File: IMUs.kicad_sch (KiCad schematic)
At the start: 15 parts, among them U501 LSM6DSL, U502 BMP390

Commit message: feat: add layout notes and net labels
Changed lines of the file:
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@@
+		)
+	)
+	(text_box "Place away from connectors, mounting holes & switching circuits."
+		(exclude_from_sim no)
+		(at 115.57 124.1808 0)
+		(size 70.485 8.773)
+		(margins 0.9525 0.9525 0.9525 0.9525)
+		(stroke
+			(width 0)
+			(type solid)
+		)
+		(fill
+			(type none)
+		)
+		(effects
+			(font
+				(face "Adwaita Sans")
+				(size 2.032 2.032)
+				(bold yes)
+			)
+			(justify left top)
 		)
 	)

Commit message: refactor: change name from FeroFly405 to FeroFlyF405
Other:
- title: FeroFly405 -> FeroFlyF405
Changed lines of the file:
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@@
 	(paper "A4")
 	(title_block
-		(title "FeroFly405")
+		(title "FeroFlyF405")
 		(date "2026-07-22")
 		(rev "1")
-		(comment 3 "GitHub: https://github.com/Ozonised/FeroFly405")
+		(comment 3 "GitHub: https://github.com/Ozonised/FeroFlyF405")
 		(comment 4 "Designed by: Farhan Khan")
 	)
@@
 		)
 		(instances
-			(project "FeroFly"
+			(project "FeroFlyF405"
 				(path "/8fea5468-8d8d-4bdb-afc0-e65b62c92669/2db1372a-2ed6-420c-af8b-d4f9c1346569/bd7b114a-6246-4c5b-8567-24e6abe0f316"
 					(reference "U501")
@@
 		)
 		(instances
-			(project "FeroFly"
+			(project "FeroFlyF405"
 				(path "/8fea5468-8d8d-4bdb-afc0-e65b62c92669/2db1372a-2ed6-420c-af8b-d4f9c1346569/bd7b114a-6246-4c5b-8567-24e6abe0f316"
 					(reference "#PWR0404")
@@
 		)
 		(instances
-			(project "FeroFly"
+			(project "FeroFlyF405"
 				(path "/8fea5468-8d8d-4bdb-afc0-e65b62c92669/2db1372a-2ed6-420c-af8b-d4f9c1346569/bd7b114a-6246-4c5b-8567-24e6abe0f316"
 					(reference "TP505")
@@
 		)
 		(instances
-			(project "FeroFly"
+			(project "FeroFlyF405"
 				(path "/8fea5468-8d8d-4bdb-afc0-e65b62c92669/2db1372a-2ed6-420c-af8b-d4f9c1346569/bd7b114a-6246-4c5b-8567-24e6abe0f316"
 					(reference "#PWR0407")
@@
 		)
 		(instances
-			(project "FeroFly"
+			(project "FeroFlyF405"
 				(path "/8fea5468-8d8d-4bdb-afc0-e65b62c92669/2db1372a-2ed6-420c-af8b-d4f9c1346569/bd7b114a-6246-4c5b-8567-24e6abe0f316"
 					(reference "C502")
@@
 		)
 		(instances
-			(project "FeroFly"
+			(project "FeroFlyF405"
 				(path "/8fea5468-8d8d-4bdb-afc0-e65b62c92669/2db1372a-2ed6-420c-af8b-d4f9c1346569/bd7b114a-6246-4c5b-8567-24e6abe0f316"
 					(reference "#PWR0409")
@@
 		)
 		(instances
-			(project "FeroFly"
+			(project "FeroFlyF405"
 				(path "/8fea5468-8d8d-4bdb-afc0-e65b62c92669/2db1372a-2ed6-420c-af8b-d4f9c1346569/bd7b114a-6246-4c5b-8567-24e6abe0f316"
 					(reference "#PWR0411")
@@
 		)
 		(instances
-			(project "FeroFly"
+			(project "FeroFlyF405"
 				(path "/8fea5468-8d8d-4bdb-afc0-e65b62c92669/2db1372a-2ed6-420c-af8b-d4f9c1346569/bd7b114a-6246-4c5b-8567-24e6abe0f316"
 					(reference "#PWR0410")
@@
 		)
 		(instances
-			(project "FeroFly"
+			(project "FeroFlyF405"
 				(path "/8fea5468-8d8d-4bdb-afc0-e65b62c92669/2db1372a-2ed6-420c-af8b-d4f9c1346569/bd7b114a-6246-4c5b-8567-24e6abe0f316"
 					(reference "R502")
@@
 		)
 		(instances
-			(project "FeroFly"
+			(project "FeroFlyF405"
 				(path "/8fea5468-8d8d-4bdb-afc0-e65b62c92669/2db1372a-2ed6-420c-af8b-d4f9c1346569/bd7b114a-6246-4c5b-8567-24e6abe0f316"
 					(reference "#PWR0403")
@@
 		)
 		(instances
-			(project "FeroFly"
+			(project "FeroFlyF405"
 				(path "/8fea5468-8d8d-4bdb-afc0-e65b62c92669/2db1372a-2ed6-420c-af8b-d4f9c1346569/bd7b114a-6246-4c5b-8567-24e6abe0f316"
 					(reference "C504")
@@
 		)
 		(instances
-			(project "FeroFly"
+			(project "FeroFlyF405"
 				(path "/8fea5468-8d8d-4bdb-afc0-e65b62c92669/2db1372a-2ed6-420c-af8b-d4f9c1346569/bd7b114a-6246-4c5b-8567-24e6abe0f316"
 					(reference "TP504")
@@
 		)
 		(instances
-			(project "FeroFly"
+			(project "FeroFlyF405"
 				(path "/8fea5468-8d8d-4bdb-afc0-e65b62c92669/2db1372a-2ed6-420c-af8b-d4f9c1346569/bd7b114a-6246-4c5b-8567-24e6abe0f316"
 					(reference "R501")
@@
 		)
 		(instances
-			(project "FeroFly"
+			(project "FeroFlyF405"
 				(path "/8fea5468-8d8d-4bdb-afc0-e65b62c92669/2db1372a-2ed6-420c-af8b-d4f9c1346569/bd7b114a-6246-4c5b-8567-24e6abe0f316"
 					(reference "#PWR0406")
@@
 		)
 		(instances
-			(project "FeroFly"
+			(project "FeroFlyF405"
 				(path "/8fea5468-8d8d-4bdb-afc0-e65b62c92669/2db1372a-2ed6-420c-af8b-d4f9c1346569/bd7b114a-6246-4c5b-8567-24e6abe0f316"
 					(reference "#PWR0415")
@@
 		)
 		(instances
-			(project "FeroFly"
+			(project "FeroFlyF405"
 				(path "/8fea5468-8d8d-4bdb-afc0-e65b62c92669/2db1372a-2ed6-420c-af8b-d4f9c1346569/bd7b114a-6246-4c5b-8567-24e6abe0f316"
 					(reference "#PWR0413")
@@
 		)
 		(instances
-			(project "FeroFly"
+			(project "FeroFlyF405"
 				(path "/8fea5468-8d8d-4bdb-afc0-e65b62c92669/2db1372a-2ed6-420c-af8b-d4f9c1346569/bd7b114a-6246-4c5b-8567-24e6abe0f316"
 					(reference "#PWR0405")
@@
 		)
 		(instances
-			(project "FeroFly"
+			(project "FeroFlyF405"
 				(path "/8fea5468-8d8d-4bdb-afc0-e65b62c92669/2db1372a-2ed6-420c-af8b-d4f9c1346569/bd7b114a-6246-4c5b-8567-24e6abe0f316"
 					(reference "#PWR0402")
@@
 		)
 		(instances
-			(project "FeroFly"
+			(project "FeroFlyF405"
 				(path "/8fea5468-8d8d-4bdb-afc0-e65b62c92669/2db1372a-2ed6-420c-af8b-d4f9c1346569/bd7b114a-6246-4c5b-8567-24e6abe0f316"
 					(reference "TP502")
@@
 		)
 		(instances
-			(project "FeroFly"
+			(project "FeroFlyF405"
 				(path "/8fea5468-8d8d-4bdb-afc0-e65b62c92669/2db1372a-2ed6-420c-af8b-d4f9c1346569/bd7b114a-6246-4c5b-8567-24e6abe0f316"
 					(reference "TP501")
@@
 		)
 		(instances
-			(project "FeroFly"
+			(project "FeroFlyF405"
 				(path "/8fea5468-8d8d-4bdb-afc0-e65b62c92669/2db1372a-2ed6-420c-af8b-d4f9c1346569/bd7b114a-6246-4c5b-8567-24e6abe0f316"
 					(reference "#PWR0408")
@@
 		)
 		(instances
-			(project "FeroFly"
+			(project "FeroFlyF405"
 				(path "/8fea5468-8d8d-4bdb-afc0-e65b62c92669/2db1372a-2ed6-420c-af8b-d4f9c1346569/bd7b114a-6246-4c5b-8567-24e6abe0f316"
 					(reference "U502")
@@
 		)
 		(instances
-			(project "FeroFly"
+			(project "FeroFlyF405"
 				(path "/8fea5468-8d8d-4bdb-afc0-e65b62c92669/2db1372a-2ed6-420c-af8b-d4f9c1346569/bd7b114a-6246-4c5b-8567-24e6abe0f316"
 					(reference "R504")
@@
 		)
 		(instances
-			(project "FeroFly"
+			(project "FeroFlyF405"
 				(path "/8fea5468-8d8d-4bdb-afc0-e65b62c92669/2db1372a-2ed6-420c-af8b-d4f9c1346569/bd7b114a-6246-4c5b-8567-24e6abe0f316"
 					(reference "C503")
@@
 		)
 		(instances
-			(project "FeroFly"
+			(project "FeroFlyF405"
 				(path "/8fea5468-8d8d-4bdb-afc0-e65b62c92669/2db1372a-2ed6-420c-af8b-d4f9c1346569/bd7b114a-6246-4c5b-8567-24e6abe0f316"
 					(reference "#PWR0414")
@@
 		)
 		(instances
-			(project "FeroFly"
+			(project "FeroFlyF405"
 				(path "/8fea5468-8d8d-4bdb-afc0-e65b62c92669/2db1372a-2ed6-420c-af8b-d4f9c1346569/bd7b114a-6246-4c5b-8567-24e6abe0f316"
 					(reference "#PWR0401")
@@
 		)
 		(instances
-			(project "FeroFly"
+			(project "FeroFlyF405"
 				(path "/8fea5468-8d8d-4bdb-afc0-e65b62c92669/2db1372a-2ed6-420c-af8b-d4f9c1346569/bd7b114a-6246-4c5b-8567-24e6abe0f316"
 					(reference "#PWR0412")
@@
 		)
 		(instances
-			(project "FeroFly"
+			(project "FeroFlyF405"
 				(path "/8fea5468-8d8d-4bdb-afc0-e65b62c92669/2db1372a-2ed6-420c-af8b-d4f9c1346569/bd7b114a-6246-4c5b-8567-24e6abe0f316"
 					(reference "C501")
@@
 		)
 		(instances
-			(project "FeroFly"
+			(project "FeroFlyF405"
 				(path "/8fea5468-8d8d-4bdb-afc0-e65b62c92669/2db1372a-2ed6-420c-af8b-d4f9c1346569/bd7b114a-6246-4c5b-8567-24e6abe0f316"
 					(reference "R503")
@@
 		)
 		(instances
-			(project "FeroFly"
+			(project "FeroFlyF405"
 				(path "/8fea5468-8d8d-4bdb-afc0-e65b62c92669/2db1372a-2ed6-420c-af8b-d4f9c1346569/bd7b114a-6246-4c5b-8567-24e6abe0f316"
 					(reference "TP503")

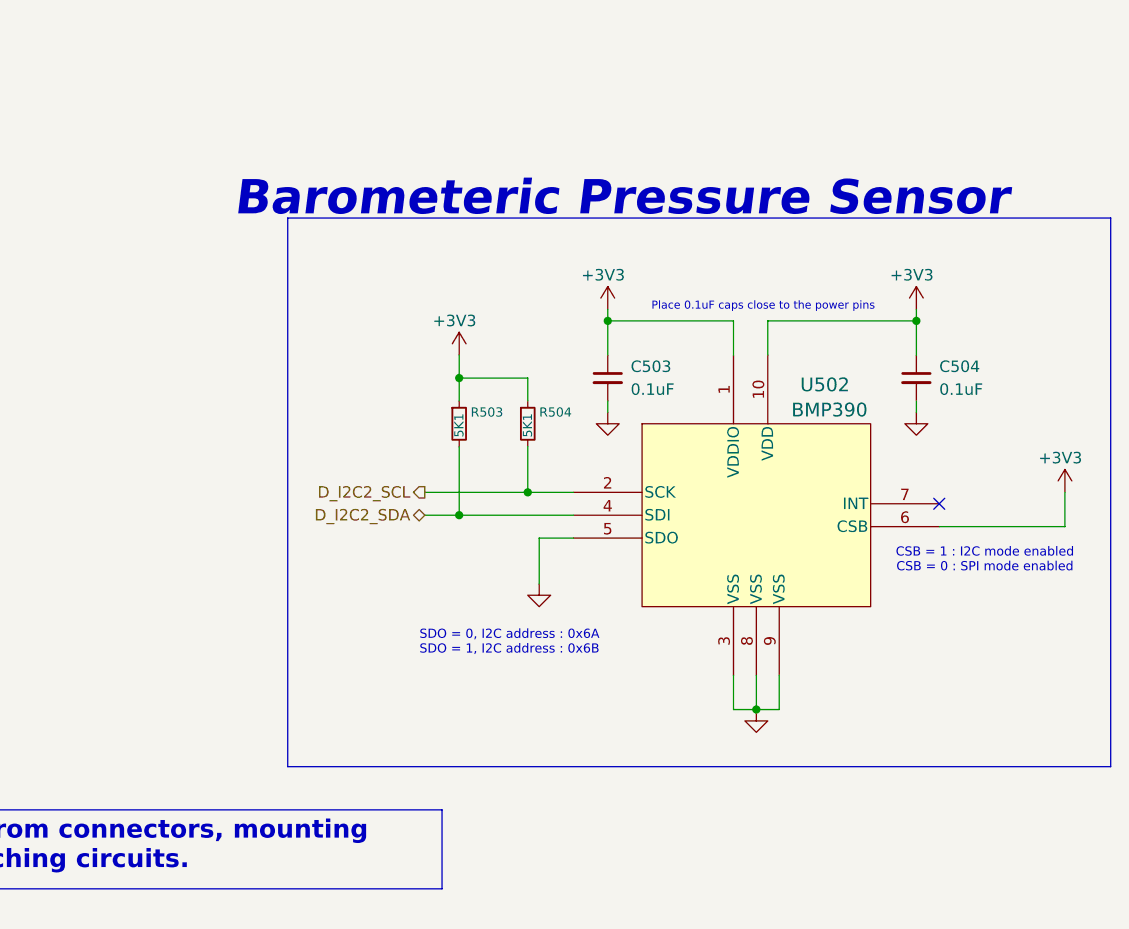
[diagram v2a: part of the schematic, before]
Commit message: refactor(hw): replace BMP390 barometer with DPS368
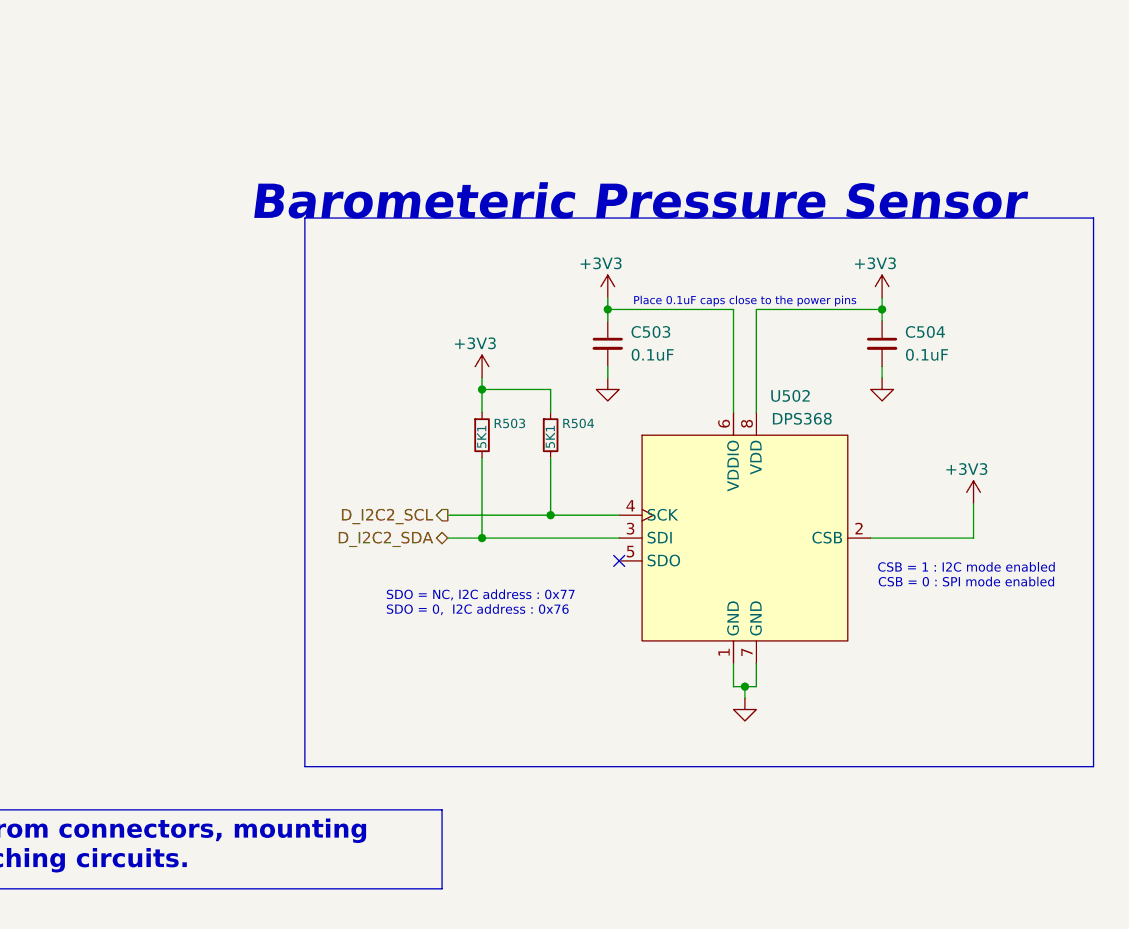
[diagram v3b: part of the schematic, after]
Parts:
- removed U502: BMP390, BMP390:10LGA_2X2X0p75_BOS, symbol BMP390:BMP390
- added U502: DPS368, Package_LGA:Bosch_LGA-8_2x2.5mm_P0.65mm_ClockwisePinNumbering, symbol DPS368:DPS368
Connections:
- net +3V3: now also U502.2 (CSB), U502.6 (VDDIO), U502.8 (VDD)
- net D_I2C2_SCL: now also U502.4 (SCK)
- net D_I2C2_SDA: now also U502.3 (SDI)
- net GND: now also U502.1 (GND), U502.7 (GND)
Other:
- note added: "SDO = NC, I2C address : 0x77 SDO = 0, I2C address : 0x76"
- note removed: "SDO = 0, I2C address : 0x6A SDO = 1, I2C address : 0x6B"

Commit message: refactor(schematic): assign net classes and fix USB net label assingment
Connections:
- net D_SPI1_CS renamed SPI1_CS
- net D_SPI1_MISO renamed SPI1_MISO
- net D_SPI1_MISOR renamed SPI1_MISOR
- net D_SPI1_MOSI renamed SPI1_MOSI
- net D_SPI1_SCK renamed SPI1_SCK
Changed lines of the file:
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@@
 		)
 	)
-	(label "D_SPI1_MISOR"
+	(label "SPI1_MISOR"
 		(at 72.39 86.36 0)
 		(effects
@@
 		)
 	)
-	(hierarchical_label "D_SPI1_MISO"
+	(hierarchical_label "SPI1_MISO"
 		(shape input)
 		(at 59.69 86.36 180)
@@
 		)
 	)
-	(hierarchical_label "D_SPI1_MOSI"
+	(hierarchical_label "SPI1_MOSI"
 		(shape input)
 		(at 59.69 96.52 180)
@@
 		)
 	)
-	(hierarchical_label "D_SPI1_CS"
+	(hierarchical_label "SPI1_CS"
 		(shape output)
 		(at 58.42 111.76 180)
@@
 		)
 	)
-	(hierarchical_label "D_SPI1_SCK"
+	(hierarchical_label "SPI1_SCK"
 		(shape output)
 		(at 59.69 99.06 180)
